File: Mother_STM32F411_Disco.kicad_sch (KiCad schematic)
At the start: 15 parts

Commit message: boceteando todavia
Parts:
- renumbered Multiplex_Audio_in to Multiplex_Audio_in1
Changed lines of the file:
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@@
 		(dnp no)
 		(fields_autoplaced yes)
-		(property "Reference" "Multiplex_Audio_in"
+		(property "Reference" "Multiplex_Audio_in1"
 			(at 90.17 36.83 0)
 			(effects
@@
 			(project ""
 				(path "/a39c1df0-9e3d-4c83-b910-4e288e398b9e"
-					(reference "Multiplex_Audio_in")
+					(reference "Multiplex_Audio_in1")
 					(unit 1)
 				)

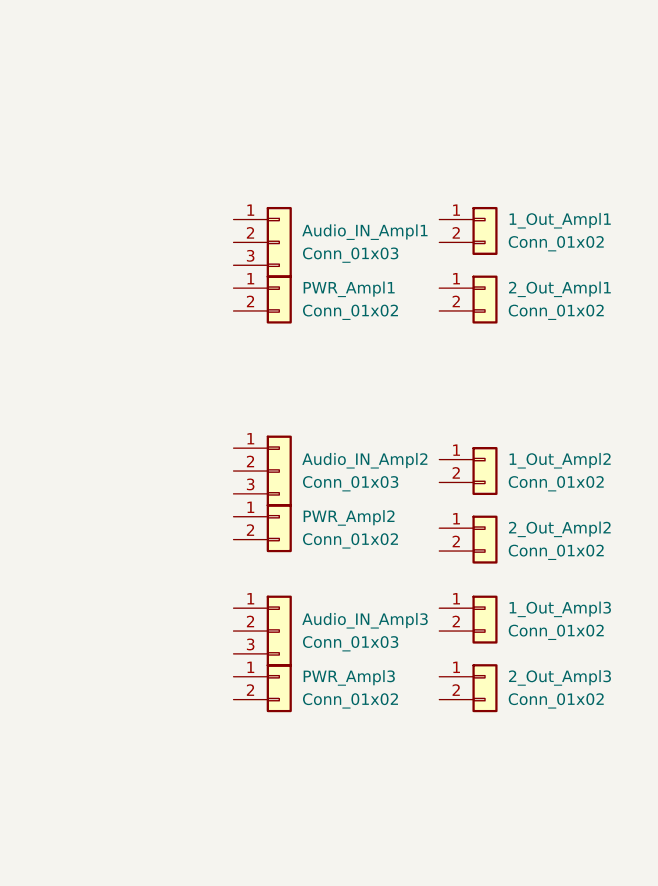
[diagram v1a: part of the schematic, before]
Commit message: SA-18: placa de esp32 devkitv1 agregada a el esquematico
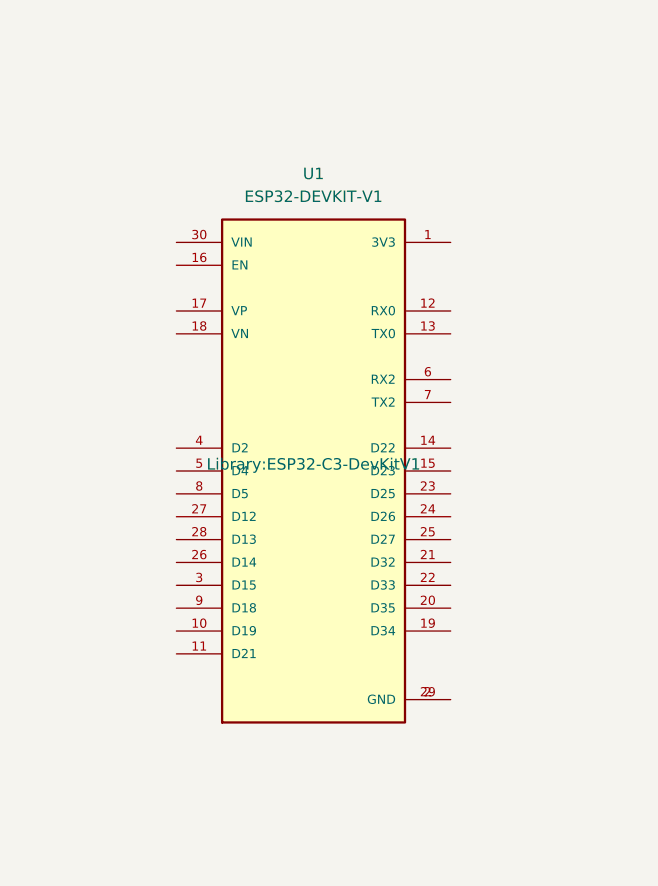
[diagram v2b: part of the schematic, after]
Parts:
- removed 1_Out_Ampl1, 1_Out_Ampl2, 1_Out_Ampl3, 2_Out_Ampl1, 2_Out_Ampl2, 2_Out_Ampl3, PWR_Ampl1, PWR_Ampl2, PWR_Ampl3: Conn_01x02, symbol Connector_Generic:Conn_01x02
- removed Audio_IN_Ampl1, Audio_IN_Ampl2, Audio_IN_Ampl3: Conn_01x03, symbol Connector_Generic:Conn_01x03
- added U1: ESP32-DEVKIT-V1, Library:ESP32-C3-DevKitV1, symbol ESP32-DEVKIT-V1:ESP32-DEVKIT-V1
- Multiplex_Audio_in1: footprint (none) -> Connector_PinHeader_1.00mm:PinHeader_2x08_P1.00mm_Vertical
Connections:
- new net: U1.2 (GND), U1.29 (GND)

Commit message: .sch mergeado
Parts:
- added 1_Out_Ampl1, 1_Out_Ampl2, 1_Out_Ampl3, 2_Out_Ampl1, 2_Out_Ampl2, 2_Out_Ampl3, PWR_Ampl1, PWR_Ampl2, PWR_Ampl3: Conn_01x02, Connector_PinSocket_2.54mm:PinSocket_1x02_P2.54mm_Vertical, symbol Connector_Generic:Conn_01x02
- added Audio_IN_Ampl1, Audio_IN_Ampl2, Audio_IN_Ampl3, Multiplex_Audio_out_1, Multiplex_Audio_out_2, Multiplex_Audio_out_3: Conn_01x03, Connector_PinSocket_2.54mm:PinSocket_1x03_P2.54mm_Vertical, symbol Connector_Generic:Conn_01x03
- added Out_Speaker_1, Out_Speaker_2, Out_Speaker_3, Out_Speaker_4, Out_Speaker_5, Out_Speaker_6: Conn_01x02, Connector_PinHeader_2.54mm:PinHeader_1x02_P2.54mm_Horizontal, symbol Connector_Generic:Conn_01x02
- added Pantalla-Botones1: Conn_01x08, Connector_PinSocket_2.54mm:PinSocket_1x08_P2.54mm_Vertical, symbol Connector_Generic:Conn_01x08
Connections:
- net 5V: now also Pantalla-Botones1.8 (Pin_8)
- net GND: now also PWR_Ampl1.1 (Pin_1), PWR_Ampl2.1 (Pin_1), PWR_Ampl3.1 (Pin_1), Pantalla-Botones1.1 (Pin_1)
- net PA8: now also Pantalla-Botones1.6 (Pin_6)
- net PC9: now also Pantalla-Botones1.7 (Pin_7)
- net PD11: now also Pantalla-Botones1.4 (Pin_4)
- net PD13: now also Pantalla-Botones1.3 (Pin_3)
- net PD14: now also Pantalla-Botones1.2 (Pin_2)
- net PD9: now also Pantalla-Botones1.5 (Pin_5)
- net VDD: now also PWR_Ampl1.2 (Pin_2), PWR_Ampl2.2 (Pin_2), PWR_Ampl3.2 (Pin_2)
- new net: 2_Out_Ampl2.1 (Pin_1), Out_Speaker_4.2 (Pin_2)
- new net: 2_Out_Ampl2.2 (Pin_2), Out_Speaker_4.1 (Pin_1)
- new net: 1_Out_Ampl2.1 (Pin_1), Out_Speaker_3.2 (Pin_2)
- new net: 1_Out_Ampl2.2 (Pin_2), Out_Speaker_3.1 (Pin_1)
- new net: 1_Out_Ampl1.1 (Pin_1), Out_Speaker_1.2 (Pin_2)
- new net: 1_Out_Ampl1.2 (Pin_2), Out_Speaker_1.1 (Pin_1)
- new net: Audio_IN_Ampl3.2 (Pin_2), Multiplex_Audio_out_3.1 (Pin_1)
- new net: Audio_IN_Ampl3.3 (Pin_3), Multiplex_Audio_out_3.2 (Pin_2)
- new net: Audio_IN_Ampl3.1 (Pin_1), Multiplex_Audio_out_3.3 (Pin_3)
- new net: 2_Out_Ampl1.1 (Pin_1), Out_Speaker_2.2 (Pin_2)
- new net: 2_Out_Ampl1.2 (Pin_2), Out_Speaker_2.1 (Pin_1)
- new net: Audio_IN_Ampl2.2 (Pin_2), Multiplex_Audio_out_2.1 (Pin_1)
- new net: Audio_IN_Ampl2.3 (Pin_3), Multiplex_Audio_out_2.2 (Pin_2)
- new net: Audio_IN_Ampl2.1 (Pin_1), Multiplex_Audio_out_2.3 (Pin_3)
- new net: 2_Out_Ampl3.2 (Pin_2), Out_Speaker_6.1 (Pin_1)
- new net: 2_Out_Ampl3.1 (Pin_1), Out_Speaker_6.2 (Pin_2)
- new net: Audio_IN_Ampl1.2 (Pin_2), Multiplex_Audio_out_1.1 (Pin_1)
- new net: Audio_IN_Ampl1.3 (Pin_3), Multiplex_Audio_out_1.2 (Pin_2)
- new net: Audio_IN_Ampl1.1 (Pin_1), Multiplex_Audio_out_1.3 (Pin_3)
- new net: 1_Out_Ampl3.2 (Pin_2), Out_Speaker_5.1 (Pin_1)
- new net: 1_Out_Ampl3.1 (Pin_1), Out_Speaker_5.2 (Pin_2)
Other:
- moved on the sheet: Conn_Der_STM_Disco1, Multiplex_Audio_in1, U1

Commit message: Merge pcb listo
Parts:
- added SRC_5V, SRC_GND: Conn_01x02, Connector_PinSocket_2.54mm:PinSocket_1x02_P2.54mm_Vertical, symbol Connector_Generic:Conn_01x02
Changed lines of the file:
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@@
+	)
+	(symbol
+		(lib_id "Connector_Generic:Conn_01x02")
+		(at 222.25 35.56 180)
+		(unit 1)
+		(exclude_from_sim no)
+		(in_bom yes)
+		(on_board yes)
+		(dnp no)
+		(fields_autoplaced yes)
+		(property "Reference" "SRC_5V"
+			(at 222.25 26.67 0)
+			(effects
+				(font
+					(size 1.27 1.27)
+				)
+			)
+		)
+		(property "Value" "Conn_01x02"
+			(at 222.25 29.21 0)
+			(effects
+				(font
+					(size 1.27 1.27)
+				)
+			)
+		)
+		(property "Footprint" "Connector_PinSocket_2.54mm:PinSocket_1x02_P2.54mm_Vertical"
+			(at 222.25 35.56 0)
+			(effects
+				(font
+					(size 1.27 1.27)
+				)
+				(hide yes)
+			)
+		)
+		(property "Datasheet" "~"
+			(at 222.25 35.56 0)
+			(effects
+				(font
+					(size 1.27 1.27)
+				)
+				(hide yes)
+			)
+		)
+		(property "Description" "Generic connector, single row, 01x02, script generated (kicad-library-utils/schlib/autogen/connector/)"
+			(at 222.25 35.56 0)
+			(effects
+				(font
+					(size 1.27 1.27)
+				)
+				(hide yes)
+			)
+		)
+		(pin "2"
+		)
+		(pin "1"
+		)
+		(instances
+			(project ""
+				(path "/a39c1df0-9e3d-4c83-b910-4e288e398b9e"
+					(reference "SRC_5V")
+					(unit 1)
+				)
+			)
+		)
 	)
 	(symbol
@@
 					(unit 1)
 				)
+			)
+		)
+	)
+	(symbol
+		(lib_id "Connector_Generic:Conn_01x02")
+		(at 222.25 48.26 180)
+		(unit 1)
+		(exclude_from_sim no)
+		(in_bom yes)
+		(on_board yes)
+		(dnp no)
+		(fields_autoplaced yes)
+		(property "Reference" "SRC_GND"
+			(at 222.25 39.37 0)
+			(effects
+				(font
+					(size 1.27 1.27)
+				)
+			)
+		)
+		(property "Value" "Conn_01x02"
+			(at 222.25 41.91 0)
+			(effects
+				(font
+					(size 1.27 1.27)
+				)
+			)
+		)
+		(property "Footprint" "Connector_PinSocket_2.54mm:PinSocket_1x02_P2.54mm_Vertical"
+			(at 222.25 48.26 0)
+			(effects
+				(font
+					(size 1.27 1.27)
+				)
+				(hide yes)
+			)
+		)
+		(property "Datasheet" "~"
+			(at 222.25 48.26 0)
+			(effects
+				(font
+					(size 1.27 1.27)
+				)
+				(hide yes)
+			)
+		)
+		(property "Description" "Generic connector, single row, 01x02, script generated (kicad-library-utils/schlib/autogen/connector/)"
+			(at 222.25 48.26 0)
+			(effects
+				(font
+					(size 1.27 1.27)
+				)
+				(hide yes)
+			)
+		)
+		(pin "2"
+		)
+		(pin "1"
+		)
+		(instances
+			(project "Mother_STM32F411_Disco"
+				(path "/a39c1df0-9e3d-4c83-b910-4e288e398b9e"
+					(reference "SRC_GND")
+					(unit 1)
+				)

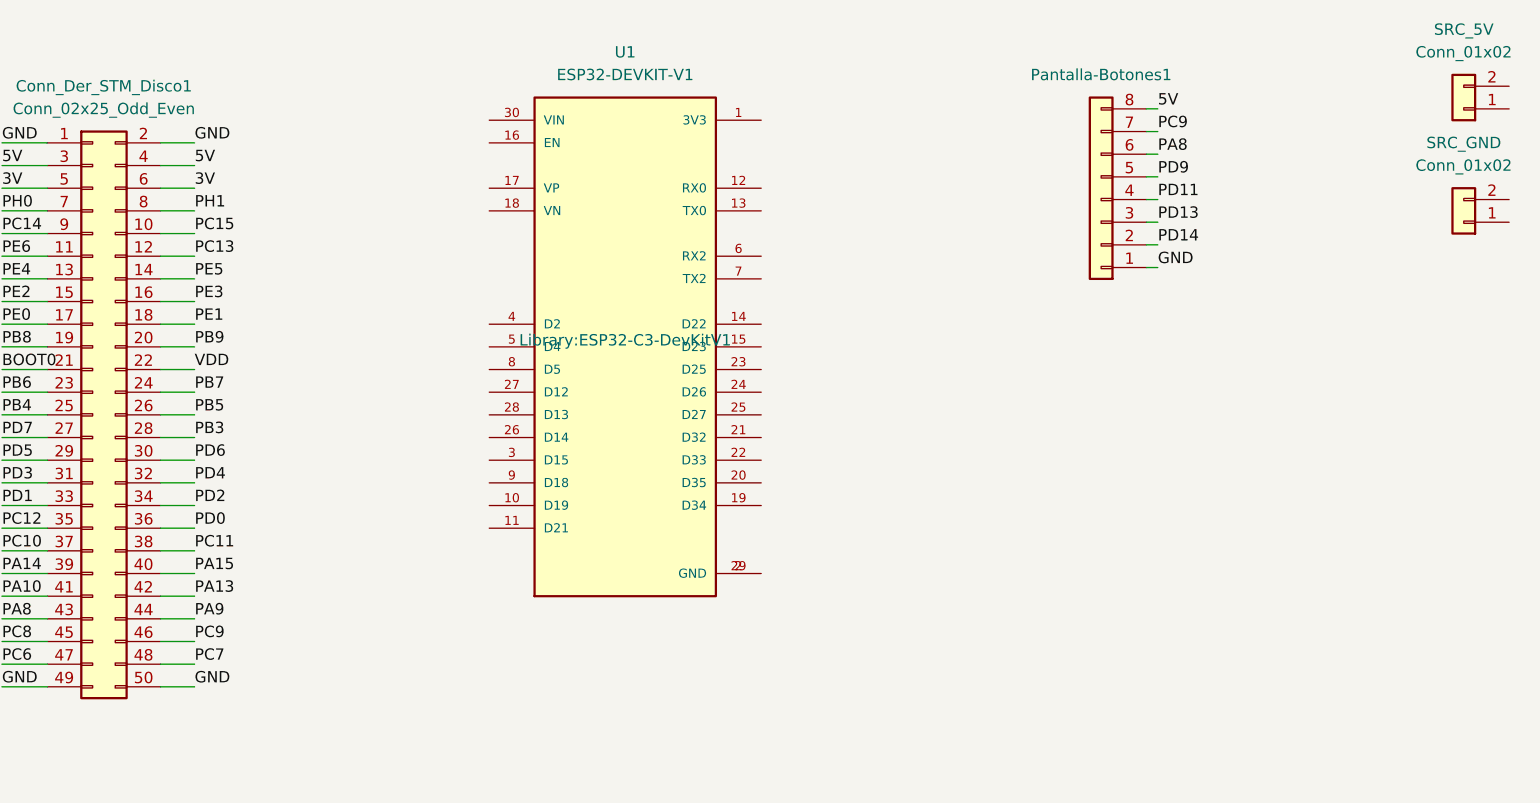
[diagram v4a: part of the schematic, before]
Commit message: UART STM conectada
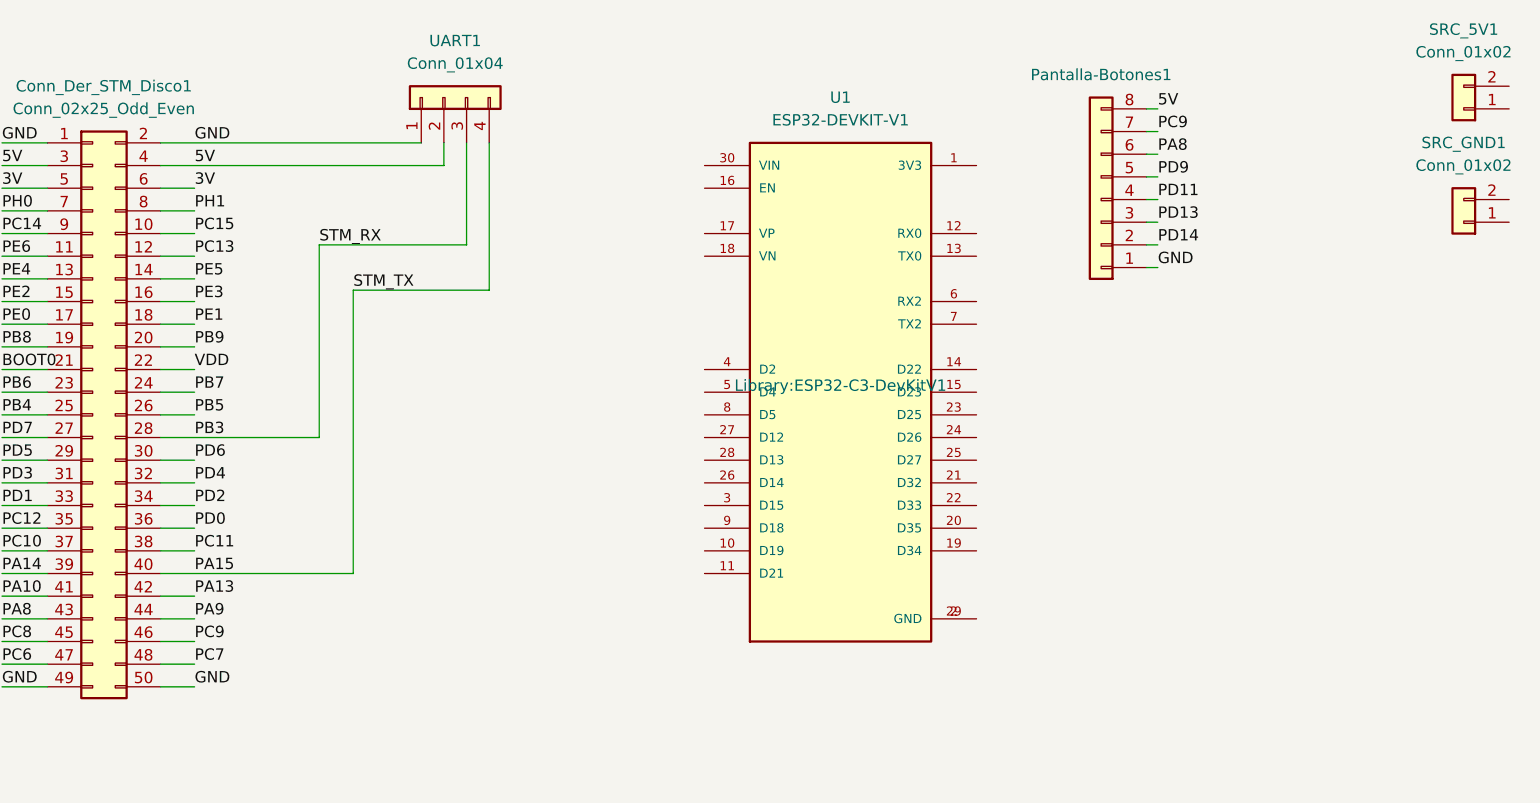
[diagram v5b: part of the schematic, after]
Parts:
- added UART1: Conn_01x04, Connector_PinSocket_2.54mm:PinSocket_1x04_P2.54mm_Horizontal, symbol Connector_Generic:Conn_01x04
- renumbered SRC_5V to SRC_5V1, SRC_GND to SRC_GND1
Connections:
- net 5V: now also UART1.2 (Pin_2)
- net GND: now also UART1.1 (Pin_1)
- net PA15: now also UART1.4 (Pin_4)
- net PB3: now also UART1.3 (Pin_3)
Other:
- moved on the sheet: U1
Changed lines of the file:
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@@
 	(wire
 		(pts
+			(xy 93.98 50.8) (xy 93.98 72.39)
+		)
+		(stroke
+			(width 0)
+			(type default)
+		)
+	)
+	(wire
+		(pts
 			(xy 58.42 77.47) (xy 63.5 77.47)
 		)
@@
 	(wire
 		(pts
+			(xy 97.79 55.88) (xy 97.79 87.63)
+		)
+		(stroke
+			(width 0)
+			(type default)
+		)
+	)
+	(wire
+		(pts
 			(xy 127 147.32) (xy 135.89 147.32)
 		)
@@
 	(wire
 		(pts
+			(xy 110.49 50.8) (xy 93.98 50.8)
+		)
+		(stroke
+			(width 0)
+			(type default)
+		)
+	)
+	(wire
+		(pts
 			(xy 43.18 53.34) (xy 48.26 53.34)
 		)
@@
 	(wire
 		(pts
-			(xy 76.2 72.39) (xy 80.01 72.39)
+			(xy 76.2 72.39) (xy 93.98 72.39)
 		)
 		(stroke
@@
 	(wire
 		(pts
-			(xy 76.2 41.91) (xy 80.01 41.91)
+			(xy 76.2 41.91) (xy 107.95 41.91)
 		)
 		(stroke
@@
 	(wire
 		(pts
+			(xy 113.03 55.88) (xy 97.79 55.88)
+		)
+		(stroke
+			(width 0)
+			(type default)
+		)
+	)
+	(wire
+		(pts
 			(xy 22.86 86.36) (xy 30.48 86.36)
 		)
@@
 	(wire
 		(pts
+			(xy 113.03 39.37) (xy 113.03 55.88)
+		)
+		(stroke
+			(width 0)
+			(type default)
+		)
+	)
+	(wire
+		(pts
 			(xy 22.86 66.04) (xy 30.48 66.04)
 		)
@@
 	(wire
 		(pts
+			(xy 110.49 39.37) (xy 110.49 50.8)
+		)
+		(stroke
+			(width 0)
+			(type default)
+		)
+	)
+	(wire
+		(pts
 			(xy 58.42 92.71) (xy 63.5 92.71)
 		)
@@
 	(wire
 		(pts
-			(xy 76.2 39.37) (xy 80.01 39.37)
+			(xy 76.2 39.37) (xy 105.41 39.37)
 		)
 		(stroke
@@
 	(wire
 		(pts
+			(xy 107.95 39.37) (xy 107.95 41.91)
+		)
+		(stroke
+			(width 0)
+			(type default)
+		)
+	)
+	(wire
+		(pts
 			(xy 43.18 101.6) (xy 48.26 101.6)
 		)
@@
 	(wire
 		(pts
-			(xy 76.2 87.63) (xy 80.01 87.63)
+			(xy 76.2 87.63) (xy 97.79 87.63)
 		)
 		(stroke
@@
 		)
 	)
+	(label "STM_TX"
+		(at 97.79 55.88 0)
+		(effects
+			(font
+				(size 1.27 1.27)
+			)
+			(justify left bottom)
+		)
+	)
 	(label "PB3"
 		(at 80.01 72.39 0)
@@
 		)
 	)
+	(label "STM_RX"
+		(at 93.98 50.8 0)
+		(effects
+			(font
+				(size 1.27 1.27)
+			)
+			(justify left bottom)
+		)
+	)
 	(label "GND"
 		(at 77.47 125.73 0)
@@
 	(symbol
 		(lib_id "ESP32-DEVKIT-V1:ESP32-DEVKIT-V1")
-		(at 128.27 62.23 0)
+		(at 152.4 67.31 0)
 		(unit 1)
 		(exclude_from_sim no)
@@
 		(fields_autoplaced yes)
 		(property "Reference" "U1"
-			(at 128.27 29.21 0)
+			(at 152.4 34.29 0)
 			(effects
 				(font
@@
 		)
 		(property "Value" "ESP32-DEVKIT-V1"
-			(at 128.27 31.75 0)
+			(at 152.4 36.83 0)
 			(effects
 				(font
@@
 		)
 		(property "Footprint" "Library:ESP32-C3-DevKitV1"
-			(at 128.27 62.23 0)
+			(at 152.4 67.31 0)
 			(effects
 				(font
@@
 		)
 		(property "Datasheet" ""
-			(at 128.27 62.23 0)
+			(at 152.4 67.31 0)
 			(effects
 				(font
@@
 		)
 		(property "Description" ""
-			(at 128.27 62.23 0)
+			(at 152.4 67.31 0)
 			(effects
 				(font
@@
 		)
 		(property "MF" "Do it"
-			(at 128.27 62.23 0)
+			(at 152.4 67.31 0)
 			(effects
 				(font
@@
 		)
 		(property "MAXIMUM_PACKAGE_HEIGHT" "6.8 mm"
-			(at 128.27 62.23 0)
+			(at 152.4 67.31 0)
 			(effects
 				(font
@@
 		)
 		(property "Package" "None"
-			(at 128.27 62.23 0)
+			(at 152.4 67.31 0)
 			(effects
 				(font
@@
 		)
 		(property "Price" "None"
-			(at 128.27 62.23 0)
+			(at 152.4 67.31 0)
 			(effects
 				(font
@@
 		)
 		(property "Check_prices" "https://www.snapeda.com/parts/ESP32-DEVKIT-V1/Do+it/view-part/?ref=eda"
-			(at 128.27 62.23 0)
+			(at 152.4 67.31 0)
 			(effects
 				(font
@@
 		)
 		(property "STANDARD" "Manufacturer Recommendations"
-			(at 128.27 62.23 0)
+			(at 152.4 67.31 0)
 			(effects
 				(font
@@
 		)
 		(property "PARTREV" "N/A"
-			(at 128.27 62.23 0)
+			(at 152.4 67.31 0)
 			(effects
 				(font
@@
 		)
 		(property "SnapEDA_Link" "https://www.snapeda.com/parts/ESP32-DEVKIT-V1/Do+it/view-part/?ref=snap"
-			(at 128.27 62.23 0)
+			(at 152.4 67.31 0)
 			(effects
 				(font
@@
 		)
 		(property "MP" "ESP32-DEVKIT-V1"
-			(at 128.27 62.23 0)
+			(at 152.4 67.31 0)
 			(effects
 				(font
@@
 		)
 		(property "Description_1" "Dual core, Wi-Fi: 2.4 GHz up to 150 Mbits/s,BLE (Bluetooth Low Energy) and legacy Bluetooth, 32 bits, Up to 240 MHz"
-			(at 128.27 62.23 0)
+			(at 152.4 67.31 0)
 			(effects
 				(font
@@
 		)
 		(property "Availability" "Not in stock"
-			(at 128.27 62.23 0)
+			(at 152.4 67.31 0)
 			(effects
 				(font
@@
 		)
 		(property "MANUFACTURER" "DOIT"
-			(at 128.27 62.23 0)
+			(at 152.4 67.31 0)
 			(effects
 				(font
@@
 		(dnp no)
 		(fields_autoplaced yes)
-		(property "Reference" "SRC_5V"
+		(property "Reference" "SRC_5V1"
 			(at 222.25 26.67 0)
 			(effects
@@
 			(project ""
 				(path "/a39c1df0-9e3d-4c83-b910-4e288e398b9e"
-					(reference "SRC_5V")
+					(reference "SRC_5V1")
 					(unit 1)
 				)
@@
 	)
 	(symbol
+		(lib_id "Connector_Generic:Conn_01x04")
+		(at 107.95 34.29 90)
+		(unit 1)
+		(exclude_from_sim no)
+		(in_bom yes)
+		(on_board yes)
+		(dnp no)
+		(fields_autoplaced yes)
+		(property "Reference" "UART1"
+			(at 109.22 27.94 90)
+			(effects
+				(font
+					(size 1.27 1.27)
+				)
+			)
+		)
+		(property "Value" "Conn_01x04"
+			(at 109.22 30.48 90)
+			(effects
+				(font
+					(size 1.27 1.27)
+				)
+			)
+		)
+		(property "Footprint" "Connector_PinSocket_2.54mm:PinSocket_1x04_P2.54mm_Horizontal"
+			(at 107.95 34.29 0)
+			(effects
+				(font
+					(size 1.27 1.27)
+				)
+				(hide yes)
+			)
+		)
+		(property "Datasheet" "~"
+			(at 107.95 34.29 0)
+			(effects
+				(font
+					(size 1.27 1.27)
+				)
+				(hide yes)
+			)
+		)
+		(property "Description" "Generic connector, single row, 01x04, script generated (kicad-library-utils/schlib/autogen/connector/)"
+			(at 107.95 34.29 0)
+			(effects
+				(font
+					(size 1.27 1.27)
+				)
+				(hide yes)
+			)
+		)
+		(pin "1"
+		)
+		(pin "3"
+		)
+		(pin "4"
+		)
+		(pin "2"
+		)
+		(instances
+			(project ""
+				(path "/a39c1df0-9e3d-4c83-b910-4e288e398b9e"
+					(reference "UART1")
+					(unit 1)
+				)
+			)
+		)
+	)
+	(symbol
 		(lib_id "Connector_Generic:Conn_01x02")
 		(at 222.25 48.26 180)
@@
 		(dnp no)
 		(fields_autoplaced yes)
-		(property "Reference" "SRC_GND"
+		(property "Reference" "SRC_GND1"
 			(at 222.25 39.37 0)
 			(effects
@@
 			(project "Mother_STM32F411_Disco"
 				(path "/a39c1df0-9e3d-4c83-b910-4e288e398b9e"
-					(reference "SRC_GND")
+					(reference "SRC_GND1")
 					(unit 1)
 				)
